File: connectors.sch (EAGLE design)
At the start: 19 parts, among them CON2 PINHEAD_1X03-2.54-RA, CON3 CON-4P-JST_GH-RA, CON4 PINHEAD_1X02-2, CON5 PINHEAD_1X02-2, CON6 PINHEAD_1X07-2, CON8 CON-4P-JST_GH-RA, IC1 TPD3S014DBVR-SOT23-6, IC3 TJA1051

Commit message: updated compnents naming. Updated production docs
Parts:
- removed C5: 4.7µF, C_digikey:4.7µF-25V_10%_X6S-0603
- removed CON3: CON-4P-JST_GH-RA, Connectors:CON-4P-JST_GH-RA
- removed IC3: TJA1051, myxa_masterlib:TJA1051
- added C2: 0.1µF, C_digikey:0.1µF-16V_10%_X7R-0402
- added CON20: PINHEAD_1X03-2.54-RA, pinhead:PINHEAD_1X03-2.54-RA
- added IC2: TPD3S014DBVR-SOT23-6, myxa_masterlib:TPD3S014DBVR-SOT23-6
- C3: value 0.1µF -> 4.7µF; device C_digikey:0.1µF-16V_10%_X7R-0402 -> C_digikey:4.7µF-25V_10%_X6S-0603
- CON2: value PINHEAD_1X03-2.54-RA -> CON-4P-JST_GH-RA; device pinhead:PINHEAD_1X03-2.54-RA -> Connectors:CON-4P-JST_GH-RA
- IC1: value TPD3S014DBVR-SOT23-6 -> TJA1051; device myxa_masterlib:TPD3S014DBVR-SOT23-6 -> myxa_masterlib:TJA1051
- renumbered C11 to C1, C7 to C4, CON8 to CON1, R10 to R2, R11 to R3, R12 to R4, R13 to R5
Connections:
- net BEC_ENABLE: now also IC2.EN; no longer IC1.EN
- net CAN1_RX: now also IC1.RXD; no longer IC3.RXD
- net CAN1_TX: now also IC1.TXD; no longer IC3.TXD
- net CAN1_VDD: now also C3.2, CON2.1, IC2.OUT; no longer C5.2, CON3.1, IC1.OUT
- net GND: now also C2.2, C3.1, CON2.4, CON2.GND, CON20.1, IC1.S, IC2.GND; no longer C3.2, C5.1, CON2.1, CON3.4, CON3.GND, IC3.GND, IC3.S
- net GPIO1: now also CON20.3; no longer CON2.3
- net N$23: now also CON2.2, IC1.CANH; no longer CON3.2, IC3.CANH
- net N$35: now also CON2.3, IC1.CANL; no longer CON3.3, IC3.CANL
- net VDD_5V: now also C2.1, CON20.2, IC1.VCC, IC1.VIO, IC2.IN; no longer C3.1, CON2.2, IC1.IN, IC3.VCC, IC3.VIO
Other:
- moved on the sheet: C3, CON2

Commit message: Library update
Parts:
- CON1, CON2: value CON-4P-JST_GH-RA -> CON-4P-TABS-JST_GH-RA; device Connectors:CON-4P-JST_GH-RA -> Connectors:CON-4P-TABS-JST_GH-RA
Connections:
- net N$23 renamed CANH
- net N$35 renamed CANL

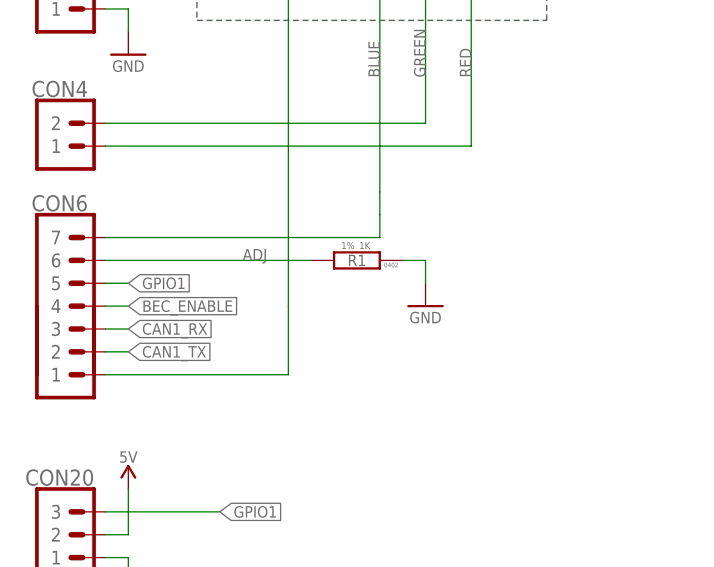
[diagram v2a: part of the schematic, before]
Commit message: Change R1 to 27K (#17)
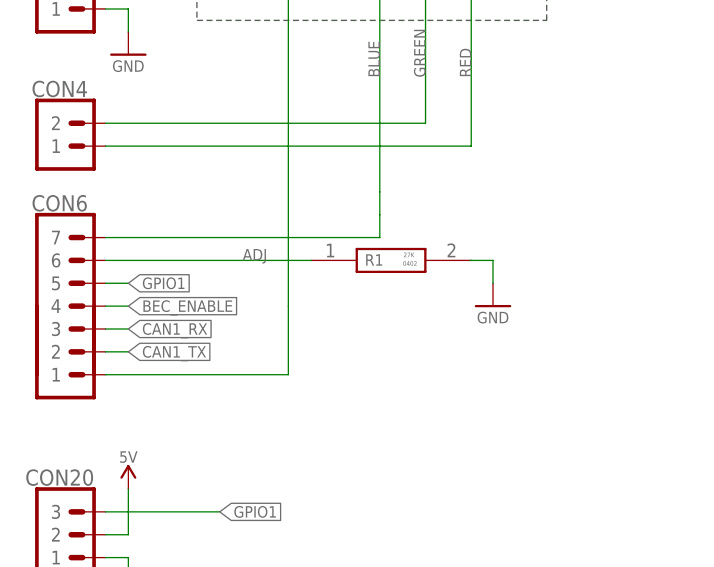
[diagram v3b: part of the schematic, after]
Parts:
- R1: value 1K -> 27K; device R_digikey:1K-1%-0402 -> RC0402FR-0727KL:RC0402FR-0727KL; DESCRIPTION (none) -> YAGEO - AF0402FR-0727KL - SMD Chip Resistor, 27 kohm, +/- 1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; HEIGHT (none) -> 0.32mm; MANUFACTURER_PART_NUMBER (none) -> AF0402FR-0727KL; PACKAGE (none) -> 0402
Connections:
- net ADJ: now also R1.1; no longer R1.2
- net GND: now also R1.2; no longer R1.1
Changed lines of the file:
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@@
 <?xml version="1.0" encoding="utf-8"?>
 <!DOCTYPE eagle SYSTEM "eagle.dtd">
-<eagle version="9.3.2">
+<eagle version="9.6.2">
 <drawing>
 <settings>
@@
 <setting verticaltext="up"/>
 </settings>
-<grid distance="0.1" unitdist="inch" unit="inch" style="lines" multiple="1" display="no" altdistance="0.01" altunitdist="inch" altunit="inch"/>
+<grid distance="0.1" unitdist="mm" unit="mm" style="lines" multiple="1" display="no" altdistance="0.001" altunitdist="mm" altunit="mm"/>
 <layers>
 <layer number="1" name="Top" color="4" fill="1" visible="no" active="no"/>
@@
 <part name="+P2" library="supply_symbols" library_urn="urn:adsk.eagle:library:5017758" deviceset="5V" device=""/>
 <part name="GND4" library="supply_symbols" library_urn="urn:adsk.eagle:library:5017758" deviceset="GND" device="" value="GND"/>
-<part name="R1" library="R_digikey" library_urn="urn:adsk.eagle:library:2539499" deviceset="1K" device="-0402" package3d_urn="urn:adsk.eagle:package:2539512/2" technology="-1%" value="1K"/>
 <part name="GND5" library="supply_symbols" library_urn="urn:adsk.eagle:library:5017758" deviceset="GND" device="" value="GND"/>
 <part name="IC2" library="myxa_masterlib" library_urn="urn:adsk.eagle:library:1040030" deviceset="TPD3S014DBVR" device="-SOT23-6" package3d_urn="urn:adsk.eagle:package:1040217/3"/>
@@
 <part name="CON1" library="Connectors" library_urn="urn:adsk.eagle:library:3750510" deviceset="CON-4P-TABS" device="-RA" package3d_urn="urn:adsk.eagle:package:1040150/6" technology="-JST_GH"/>
 <part name="CON2" library="Connectors" library_urn="urn:adsk.eagle:library:3750510" deviceset="CON-4P-TABS" device="-RA" package3d_urn="urn:adsk.eagle:package:1040150/6" technology="-JST_GH"/>
+<part name="R1" library="RC0402FR-0727KL" deviceset="RC0402FR-0727KL" device="" value="27K">
+<attribute name="DESCRIPTION" value="YAGEO - AF0402FR-0727KL - SMD Chip Resistor, 27 kohm, +/- 1%, 62.5 mW, 0402 [1005 Metric], Thick Film, General Purpose"/>
+<attribute name="HEIGHT" value="0.32mm"/>
+<attribute name="MANUFACTURER_PART_NUMBER" value="AF0402FR-0727KL"/>
+<attribute name="PACKAGE" value="0402"/>
+</part>
 </parts>
 <sheets>
@@
 <attribute name="VALUE" x="38.1" y="11.43" size="1.27" layer="96" font="vector" ratio="15" align="center"/>
 </instance>
-<instance part="R1" gate="G$1" x="63.5" y="50.8" smashed="yes" rot="R180">
-<attribute name="NAME" x="63.5" y="50.8" size="1.27" layer="95" rot="R180" align="center"/>
-<attribute name="VALUE" x="63.754" y="52.832" size="0.762" layer="96" rot="R180" align="bottom-right"/>
-<attribute name="PACKAGE" x="67.31" y="50.292" size="0.508" layer="95" rot="R180" align="center"/>
-<attribute name="TOLERANCE" x="63.246" y="52.832" size="0.762" layer="96" rot="R180"/>
-</instance>
-<instance part="GND5" gate="1" x="71.12" y="45.72" smashed="yes">
-<attribute name="VALUE" x="71.12" y="44.45" size="1.27" layer="96" font="vector" ratio="15" align="center"/>
+<instance part="GND5" gate="1" x="78.62" y="45.72" smashed="yes">
+<attribute name="VALUE" x="78.62" y="44.45" size="1.27" layer="96" font="vector" ratio="15" align="center"/>
 </instance>
 <instance part="IC2" gate="G$1" x="137.16" y="58.42" smashed="yes">
@@
 <attribute name="NAME" x="176.53" y="92.71" size="1.778" layer="95" font="vector" ratio="15" rot="R90" align="center"/>
 </instance>
+<instance part="R1" gate="G$1" x="58.4" y="50.8" smashed="yes">
+<attribute name="NAME" x="64.37" y="50.85" size="1.27" layer="95" align="center-left"/>
+<attribute name="VALUE" x="68.67" y="51.41" size="0.508" layer="96" align="center-left"/>
+<attribute name="PACKAGE" x="68.6" y="50.2" size="0.508" layer="96"/>
+</instance>
 </instances>
 <busses>
@@
 <segment>
 <pinref part="GND5" gate="1" pin="GND"/>
-<wire x1="71.12" y1="48.26" x2="71.12" y2="50.8" width="0.1524" layer="91"/>
-<pinref part="R1" gate="G$1" pin="1"/>
-<wire x1="71.12" y1="50.8" x2="68.58" y2="50.8" width="0.1524" layer="91"/>
+<wire x1="78.62" y1="48.26" x2="78.62" y2="50.8" width="0.1524" layer="91"/>
+<wire x1="78.62" y1="50.8" x2="76.18" y2="50.8" width="0.1524" layer="91"/>
+<pinref part="R1" gate="G$1" pin="2"/>
+<wire x1="76.18" y1="50.8" x2="76.08" y2="50.8" width="0.1524" layer="91"/>
 </segment>
 <segment>
@@
 <net name="ADJ" class="0">
 <segment>
-<pinref part="R1" gate="G$1" pin="2"/>
-<wire x1="35.56" y1="50.8" x2="58.42" y2="50.8" width="0.1524" layer="91"/>
+<wire x1="35.56" y1="50.8" x2="58.4" y2="50.8" width="0.1524" layer="91"/>
 <label x="50.8" y="50.8" size="1.27" layer="95"/>
 <pinref part="CON6" gate="G$1" pin="6"/>
-</segment>
-</net>
+<pinref part="R1" gate="G$1" pin="1"/>
+<wire x1="58.4" y1="50.8" x2="58.42" y2="50.8" width="0.1524" layer="91"/>
+</segment>
+</net>

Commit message: updated attributes (#19)
added MANF and MANF# attributes to the connectors and powerstage schematics
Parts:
- R1: MANF (none) -> YAGEO; MANF# (none) -> AF0402FR-0727KL
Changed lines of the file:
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@@
 <attribute name="DESCRIPTION" value="YAGEO - AF0402FR-0727KL - SMD Chip Resistor, 27 kohm, +/- 1%, 62.5 mW, 0402 [1005 Metric], Thick Film, General Purpose"/>
 <attribute name="HEIGHT" value="0.32mm"/>
+<attribute name="MANF" value="YAGEO"/>
+<attribute name="MANF#" value="AF0402FR-0727KL"/>
 <attribute name="MANUFACTURER_PART_NUMBER" value="AF0402FR-0727KL"/>
 <attribute name="PACKAGE" value="0402"/>
@@
 <attribute name="VALUE" x="68.67" y="51.41" size="0.508" layer="96" align="center-left"/>
 <attribute name="PACKAGE" x="68.6" y="50.2" size="0.508" layer="96"/>
+<attribute name="MANF" x="58.4" y="50.8" size="1.778" layer="96" display="off"/>
+<attribute name="MANF#" x="58.4" y="50.8" size="1.778" layer="96" display="off"/>
 </instance>
 </instances>
